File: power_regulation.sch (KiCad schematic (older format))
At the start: 2 parts

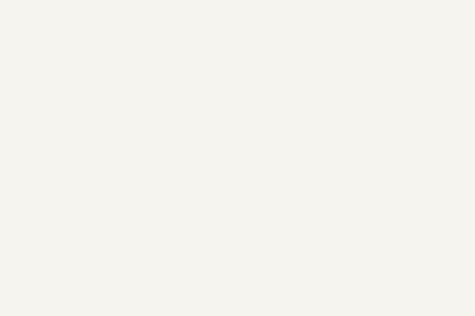
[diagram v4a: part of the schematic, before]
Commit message: revised LED parts to match reality
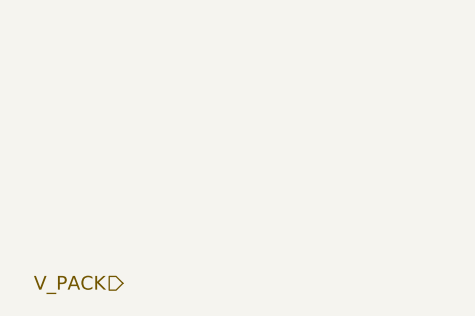
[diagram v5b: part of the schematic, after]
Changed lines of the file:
@@
 Sheet 6 14
 Title ""
-Date "17 nov 2013"
+Date "18 nov 2013"
 Rev ""
 Comp ""
@@
 	1    0    0    -1
 $EndComp
+Text HLabel 2300 3600 0    60   Input ~ 0
+V_PACK
 $EndSCHEMATC
